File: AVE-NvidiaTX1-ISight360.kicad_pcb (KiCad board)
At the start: 2 copper layers, 71.1 x 106.7 mm, 22 parts, among them P201 CONN_02X20, P401 Ultrasonic 1, P402 Ultrasonic2, P403 Ultrasonic3, P404 Ultrasonic4, P405 Ultrasonic5, P406 Ultrasonic6, U301 CD4051B, U302 DRV2605L(breakout), U303 DRV2605L(breakout)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

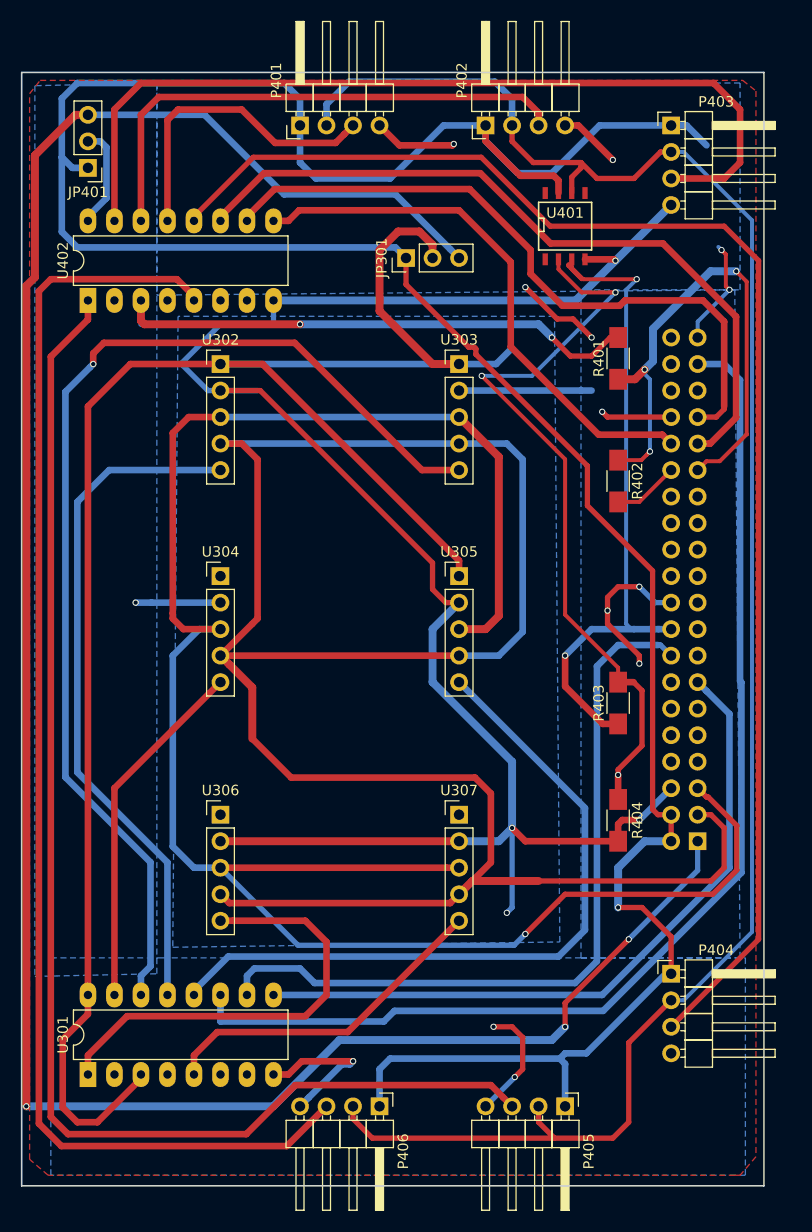
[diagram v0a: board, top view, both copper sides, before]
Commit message: Redesign - Rev B Board
Smaller Board, more symmetric, will be more stable
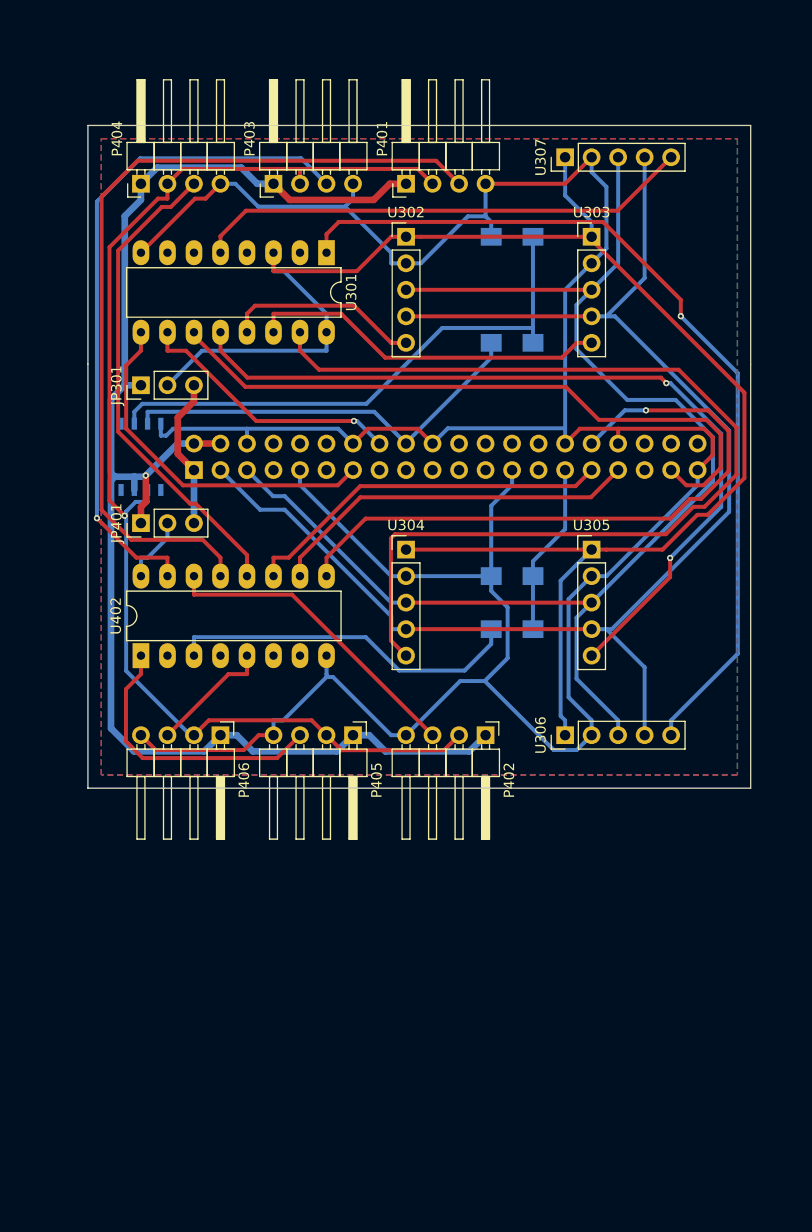
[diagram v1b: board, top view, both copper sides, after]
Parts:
- R401, R402, R403, R404, U401: moved to B.Cu
- moved P404 91.2 mm to (121.9, 46.2), turned to 90 degrees
- moved U301 82.0 mm to (139.7, 52.8), turned to 270 degrees
- moved U307 63.8 mm to (162.6, 43.7), turned to 90 degrees
- moved P201 59.9 mm to (127.0, 73.7), turned to 270 degrees
- moved P402 58.4 mm to (154.9, 99.1), turned to 270 degrees
- moved R404 56.8 mm to (157.5, 51.3), turned to 180 degrees
- moved U401 46.3 mm to (121.9, 72.4)
- moved P405 41.0 mm to (142.2, 99.1)
- moved P406 38.7 mm to (129.5, 99.1)
- moved P403 38.5 mm to (134.6, 46.2), turned to 90 degrees
- moved R403 36.0 mm to (157.5, 61.5), turned to 0 degrees
- moved JP401 34.4 mm to (121.9, 78.7), turned to 90 degrees
- moved U402 34.4 mm to (121.9, 91.4)
- moved U306 33.9 mm to (162.6, 99.1), turned to 90 degrees
- moved JP301 28.2 mm to (121.9, 65.5)
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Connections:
- P201 pad 17: /GPIO Breakout/3.3V -> /GPIO Breakout/Unused-3.3V
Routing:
- net /GPIO Breakout/3.3V: track 217.2 -> 14.5 mm, vias 3 -> 0
- net /GPIO Breakout/5V: track 265.5 -> 140.7 mm
- net /UltrasonicSensorBank/Echo6: track 126.2 -> 11.8 mm
- net /UltrasonicSensorBank/Echo5: track 127.4 -> 27.1 mm
- net /UltrasonicSensorBank/Echo4: track 137.8 -> 46.5 mm
- net Net-(U301-Pad14): track 106.9 -> 34.6 mm, vias 1 -> 0
- net /SDA: track 202.5 -> 132.1 mm
- net /SCL: track 193.0 -> 128.3 mm, vias 1 -> 0
- net Net-(U301-Pad15): track 34.2 -> 98.6 mm
- net /UltrasonicSensorBank/Ultrasonic_Trigger: track 181.7 -> 119.1 mm, vias 0 -> 1
- net /UltrasonicSensorBank/Echo1: track 29.9 -> 81.7 mm
- net /GPIO Breakout/GPIO37: track 73.7 -> 25.8 mm, vias 0 -> 1
- net Net-(U301-Pad13): track 65.8 -> 18.8 mm
- net /GPIO Breakout/GPIO187: track 110.3 -> 64.0 mm
- net Net-(U301-Pad1): track 43.2 -> 85.9 mm, vias 0 -> 1
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- removed copper zone on B.Cu, net /HapticMotorBank/M-Power
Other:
- board size 71.1 x 106.7 mm -> 63.5 x 63.5 mm
- net class Default: clearance 0.508 -> 0.381; trace_width 0.508 -> 0.381
- net class Large added: clearance 0.381, trace_width 0.635, via_dia 0.6, via_drill 0.4
- net class Larger removed
- net class Largest removed
- net class Small: clearance 0.508 -> 0.381; trace_width 0.381 -> 0.254
- rule pad_to_mask_clearance: 0.2 -> 0
- rule trace_clearance: 0.508 -> 0.381
- rule trace_min: 0.381 -> 0.254

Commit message: Rev C Update
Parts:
- added P501: Sensor Breakout, Pin_Headers:Pin_Header_Angled_2x09_Pitch2.54mm, F.Cu at (167.6, 83.8)
- moved U305 33.6 mm to (158.8, 114.3), turned to 90 degrees
- moved U306 29.3 mm to (133.3, 96.5), turned to 0 degrees
- moved P402 24.0 mm to (134.6, 111.8)
- moved R402 18.3 mm to (147.3, 99.1)
- moved R401 18.3 mm to (147.3, 104.1)
- moved P405 14.8 mm to (149.9, 111.8)
- moved P406 13.7 mm to (121.9, 110.5), turned to 180 degrees
- moved P403 5.11 mm to (129.5, 45.7)
- moved R403 3.81 mm to (161.3, 61.5)
- moved R404 3.81 mm to (161.3, 51.3)
- moved U302 3.81 mm to (151.1, 51.3)
- moved U303 3.81 mm to (168.9, 51.3)
- moved P404 3.30 mm to (121.9, 49.5), turned to 180 degrees
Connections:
- net /UltrasonicSensorBank/Echo1 renamed /Echo1
- net /UltrasonicSensorBank/Echo2 renamed /Echo2
- net /UltrasonicSensorBank/Echo3 renamed /Echo3
- net /UltrasonicSensorBank/Echo4 renamed /Echo4
- net /UltrasonicSensorBank/Echo5 renamed /Echo5
- net /UltrasonicSensorBank/Echo6 renamed /Echo6
- net /UltrasonicSensorBank/Ultrasonic_Trigger renamed /UltrasonicTigger
- net Net-(U301-Pad1) renamed /Mtrigger5
- net Net-(U301-Pad12) renamed /Mtrigger4
- net Net-(U301-Pad13) renamed /Mtrigger1
- net Net-(U301-Pad14) renamed /Mtrigger2
- net Net-(U301-Pad15) renamed /Mtrigger3
- net Net-(U301-Pad5) renamed /Mtrigger6
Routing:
- net /Mtrigger5: track 85.9 -> 159.3 mm, vias 1 -> 0
- net /SCL: track 128.3 -> 198.0 mm, vias 0 -> 2
- net /SDA: track 132.1 -> 199.3 mm
- net /Mtrigger6: track 47.9 -> 110.3 mm
- net /Mtrigger1: track 18.8 -> 76.9 mm, vias 0 -> 2
- net /Echo6: track 11.8 -> 69.7 mm
- net /GPIO Breakout/3.3V: track 14.5 -> 67.7 mm, vias 0 -> 4
- net /Echo4: track 46.5 -> 98.6 mm, vias 0 -> 1
- net /Echo2: track 30.2 -> 81.7 mm, vias 0 -> 2
- net GND: track 289.8 -> 335.1 mm, vias 0 -> 5
- net /Mtrigger2: track 34.6 -> 78.4 mm, vias 0 -> 1
- net /GPIO Breakout/5V: track 140.7 -> 184.0 mm, vias 1 -> 3
- net /Echo5: track 27.1 -> 64.5 mm
- net /Echo3: track 65.2 -> 101.9 mm
- net Net-(R403-Pad2): track 52.8 -> 83.2 mm
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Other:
- board size 63.5 x 63.5 mm -> 67.3 x 76.2 mm

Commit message: Rev C Final: PDFs, 3D Images, Silkscreens all updated
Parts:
- added G***: LOGO, Logo:Logo-PCB, F.Cu at (180.3, 49.3)
- JP401: value Usonic Power Select -> Sensor Power Select
- P201: value CONN_02X20 -> GPIO Breakout
- U302: value DRV2605L(breakout) -> Motor 1
- U303: value DRV2605L(breakout) -> Motor 2
- U304: value DRV2605L(breakout) -> Motor 4
- U305: value DRV2605L(breakout) -> Motor 6
- U306: value DRV2605L(breakout) -> Motor 5
- U307: value DRV2605L(breakout) -> Motor 3
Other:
- board text added: "Designed by: Christian Aguilar"
- board text added: "Rev C Board"
